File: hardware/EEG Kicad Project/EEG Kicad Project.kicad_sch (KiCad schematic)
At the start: 0 parts

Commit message: Added uC and started organizing schematic into sections: Power, uC, Analog
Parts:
- added U1: STM32F446RETx, Package_QFP:LQFP-64_10x10mm_P0.5mm, symbol MCU_ST_STM32F4:STM32F446RETx
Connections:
- new net GND: U1.18 (VSS), U1.31 (VSS), U1.47 (VSS), U1.63 (VSS)
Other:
- note added: "ADS1299"
- note added: "Power supply section"
- note added: "STM32"

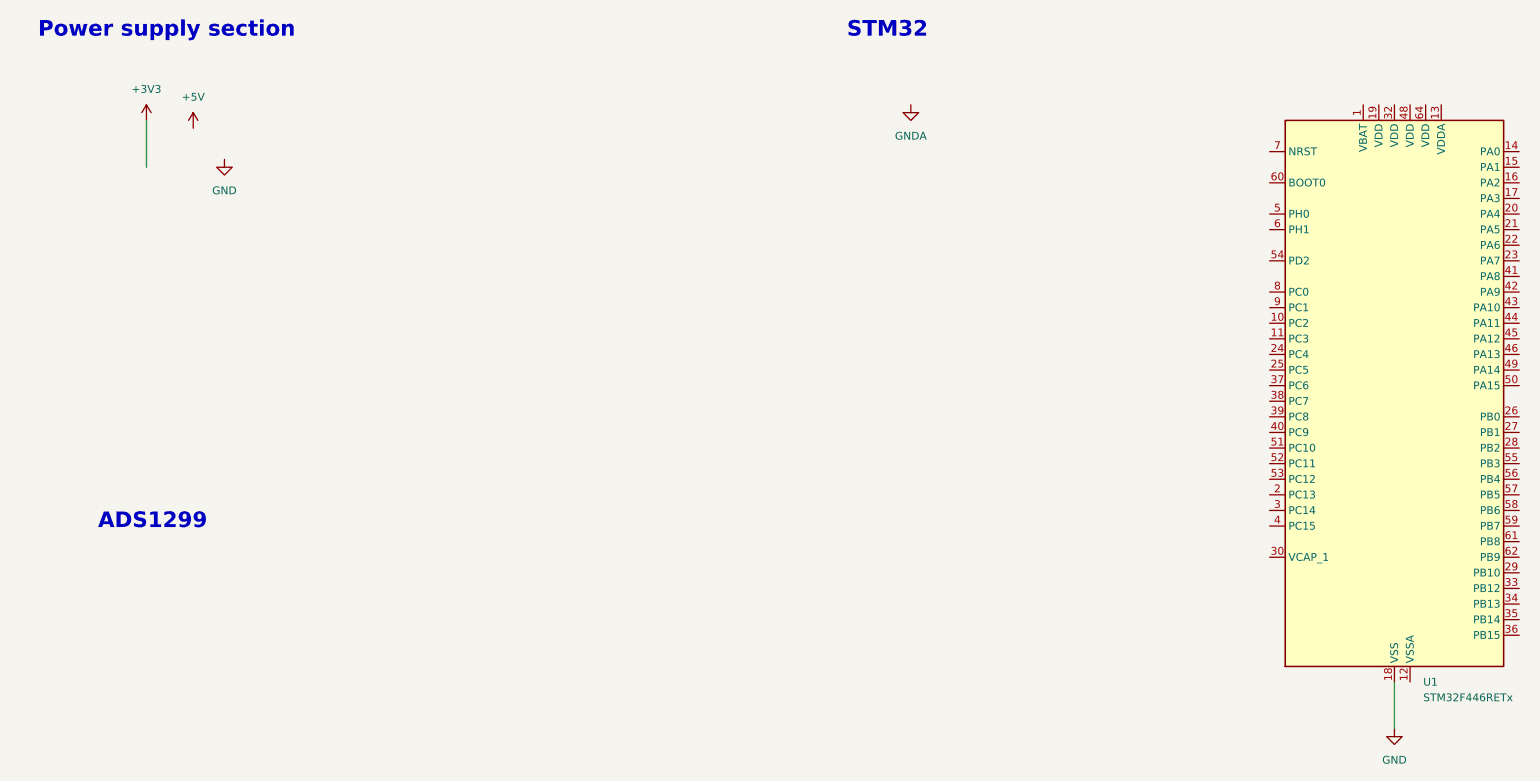
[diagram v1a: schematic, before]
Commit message: Added datasheet, modify STM32 pinout in MX, added labels on schematic, added STM32 hierarch sheet
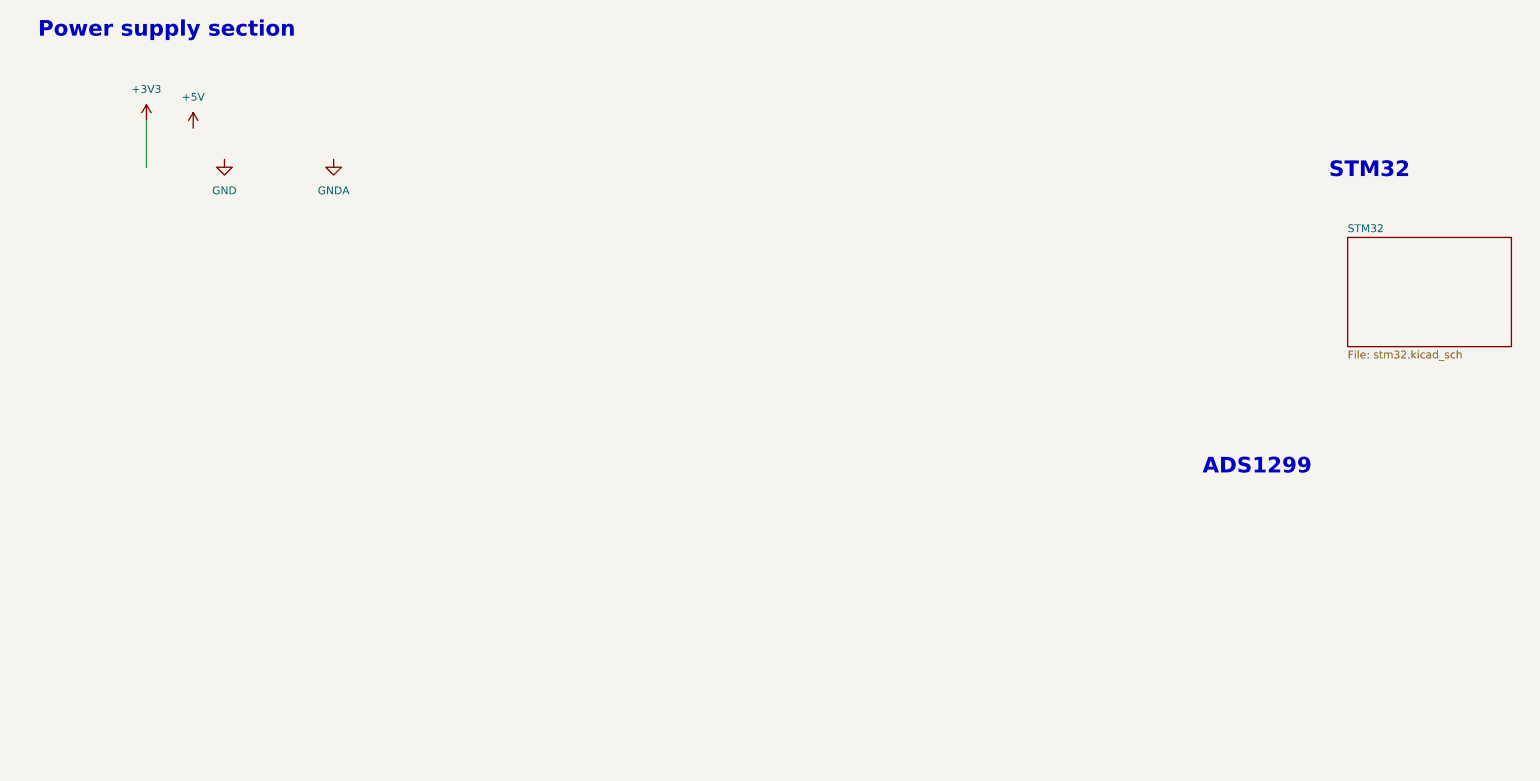
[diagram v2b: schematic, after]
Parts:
- removed U1: STM32F446RETx, Package_QFP:LQFP-64_10x10mm_P0.5mm, symbol MCU_ST_STM32F4:STM32F446RETx
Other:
- added sheet STM32 (stm32.kicad_sch)
